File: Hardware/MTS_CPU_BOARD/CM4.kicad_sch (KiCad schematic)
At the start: 1 part

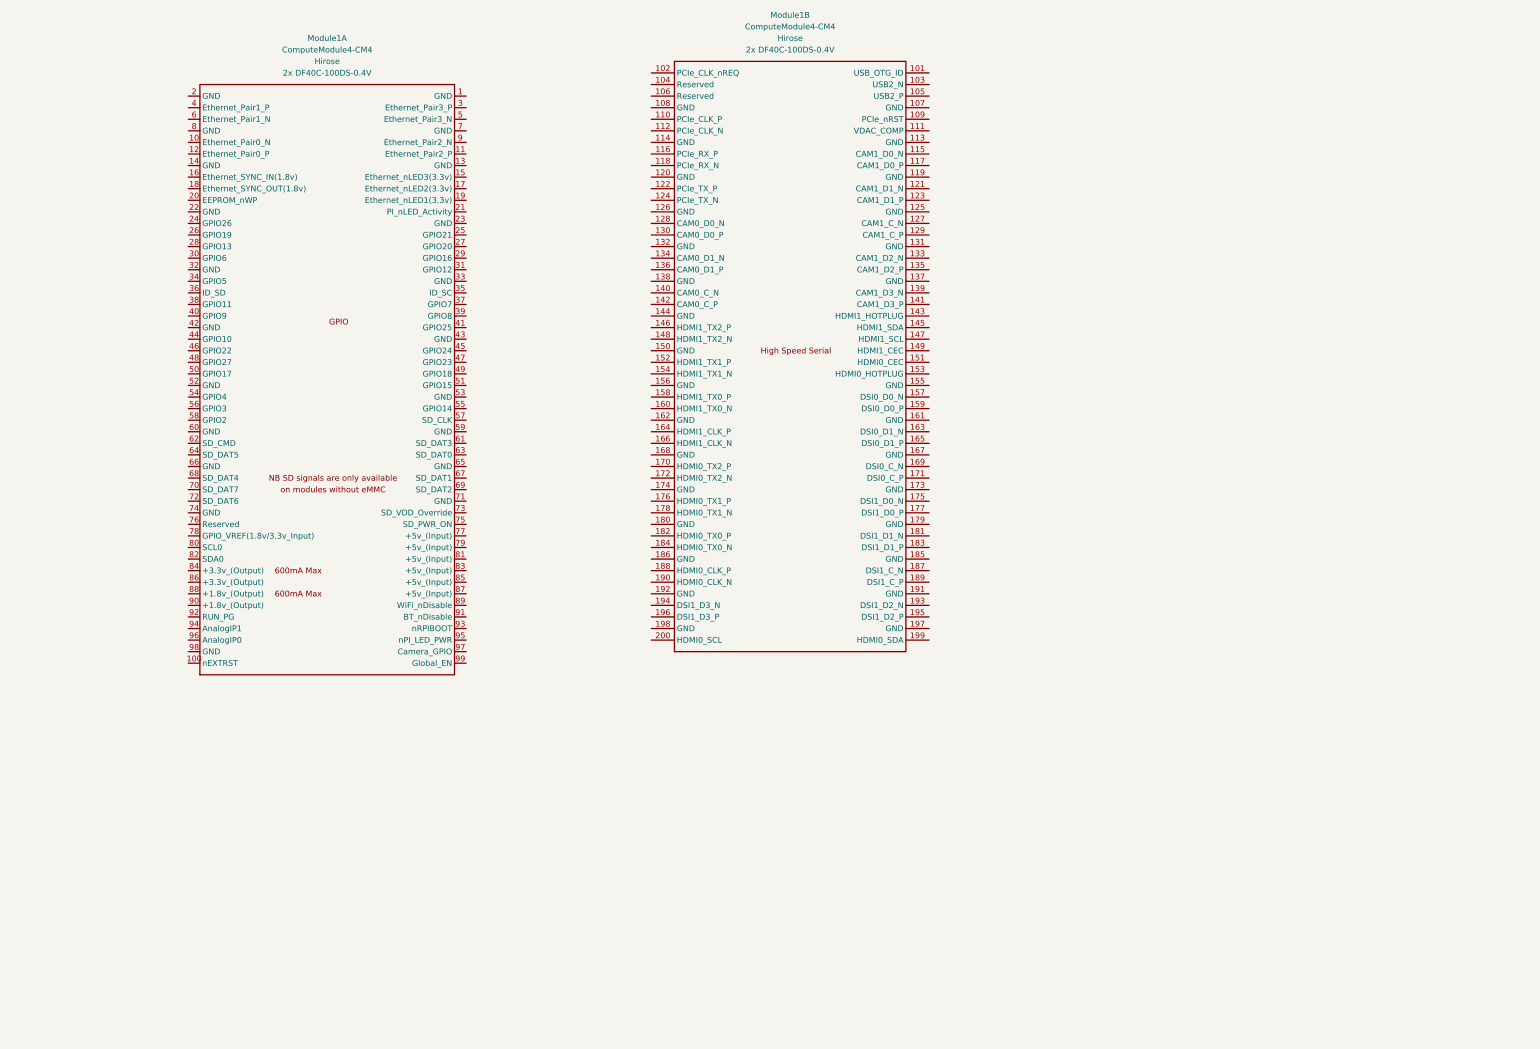
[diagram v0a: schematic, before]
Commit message: Add EtherCAT
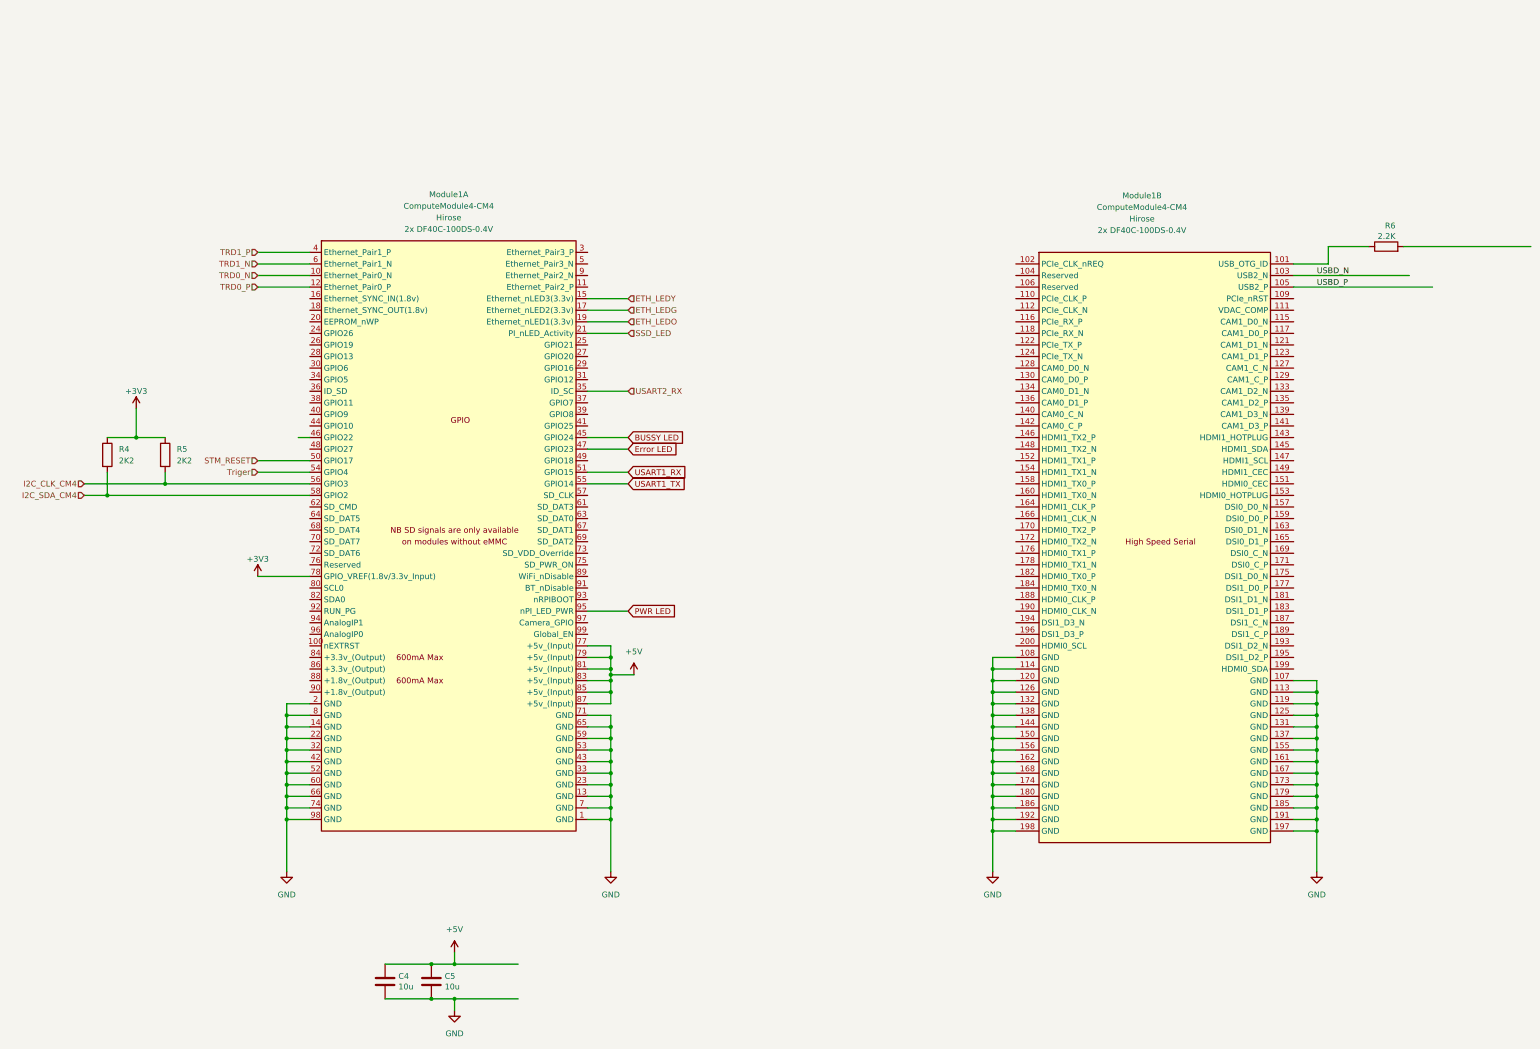
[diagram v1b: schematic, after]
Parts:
- added C4, C5: 10u, Capacitor_SMD:C_0805_2012Metric, symbol Device:C
- added R4, R5: 2K2, Resistor_SMD:R_0603_1608Metric, symbol Device:R
- added R6: 2.2K, Resistor_SMD:R_0603_1608Metric, symbol Device:R
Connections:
- net GND: now reaches Module1.1 (GND)
- net GND: now also Module1.107 (GND), Module1.108 (GND), Module1.113 (GND), Module1.114 (GND), Module1.119 (GND), Module1.120 (GND), Module1.125 (GND), Module1.126 (GND), Module1.13 (GND), Module1.131 (GND), Module1.132 (GND), Module1.137 (GND), Module1.138 (GND), Module1.14 (GND), Module1.144 (GND), Module1.150 (GND), Module1.155 (GND), Module1.156 (GND), Module1.161 (GND), Module1.162 (GND), Module1.167 (GND), Module1.168 (GND), Module1.173 (GND), Module1.174 (GND), Module1.179 (GND), Module1.180 (GND), Module1.185 (GND), Module1.186 (GND), Module1.191 (GND), Module1.192 (GND), Module1.197 (GND), Module1.198 (GND), Module1.2 (GND), Module1.22 (GND), Module1.23 (GND), Module1.32 (GND), Module1.33 (GND), Module1.42 (GND), Module1.43 (GND), Module1.52 (GND), Module1.53 (GND), Module1.59 (GND), Module1.60 (GND), Module1.65 (GND), Module1.66 (GND), Module1.7 (GND), Module1.71 (GND), Module1.74 (GND), Module1.8 (GND), Module1.98 (GND), C4.2, C5.2
- net TRD0_N: now reaches Module1.10 (Ethernet_Pair0_N)
- net TRD0_P: now reaches Module1.12 (Ethernet_Pair0_P)
- net ETH_LEDY: now reaches Module1.15 (Ethernet_nLED3(3.3v))
- net ETH_LEDG: now reaches Module1.17 (Ethernet_nLED2(3.3v))
- net ETH_LEDO: now reaches Module1.19 (Ethernet_nLED1(3.3v))
- net SSD_LED: now reaches Module1.21 (PI_nLED_Activity)
- net USART2_RX: now reaches Module1.35 (ID_SC)
- net TRD1_P: now reaches Module1.4 (Ethernet_Pair1_P)
- net BUSSY LED: now reaches Module1.45 (GPIO24)
- net Error LED: now reaches Module1.47 (GPIO23)
- net STM_RESET: now reaches Module1.50 (GPIO17)
- net USART1_RX: now reaches Module1.51 (GPIO15)
- net Triger: now reaches Module1.54 (GPIO4)
- net USART1_TX: now reaches Module1.55 (GPIO14)
- net I2C_CLK_CM4: now reaches Module1.56 (GPIO3)
- net I2C_CLK_CM4: now also R5.2
- net I2C_SDA_CM4: now reaches Module1.58 (GPIO2)
- net I2C_SDA_CM4: now also R4.2
- net TRD1_N: now reaches Module1.6 (Ethernet_Pair1_N)
- net +5V: now reaches Module1.77 (+5v_(Input))
- net +5V: now also Module1.79 (+5v_(Input)), Module1.81 (+5v_(Input)), Module1.83 (+5v_(Input)), Module1.85 (+5v_(Input)), Module1.87 (+5v_(Input)), C4.1, C5.1
- net +3V3: now reaches Module1.78 (GPIO_VREF(1.8v/3.3v_Input))
- net +3V3: now also R4.1, R5.1
- net PWR LED: now reaches Module1.95 (nPI_LED_PWR)
- net at Module1.101 (USB_OTG_ID): now also R6.1
- net USBD_N: now reaches Module1.103 (USB2_N)
- net USBD_P: now reaches Module1.105 (USB2_P)

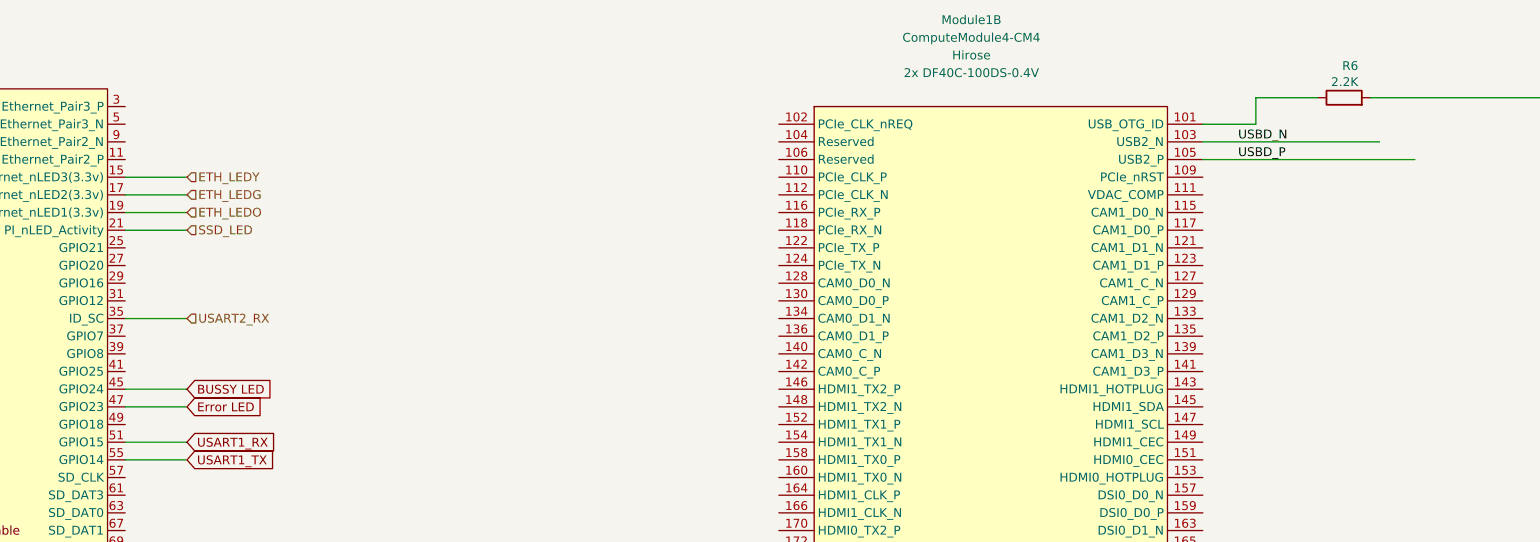
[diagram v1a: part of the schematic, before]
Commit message: Add status Led´s
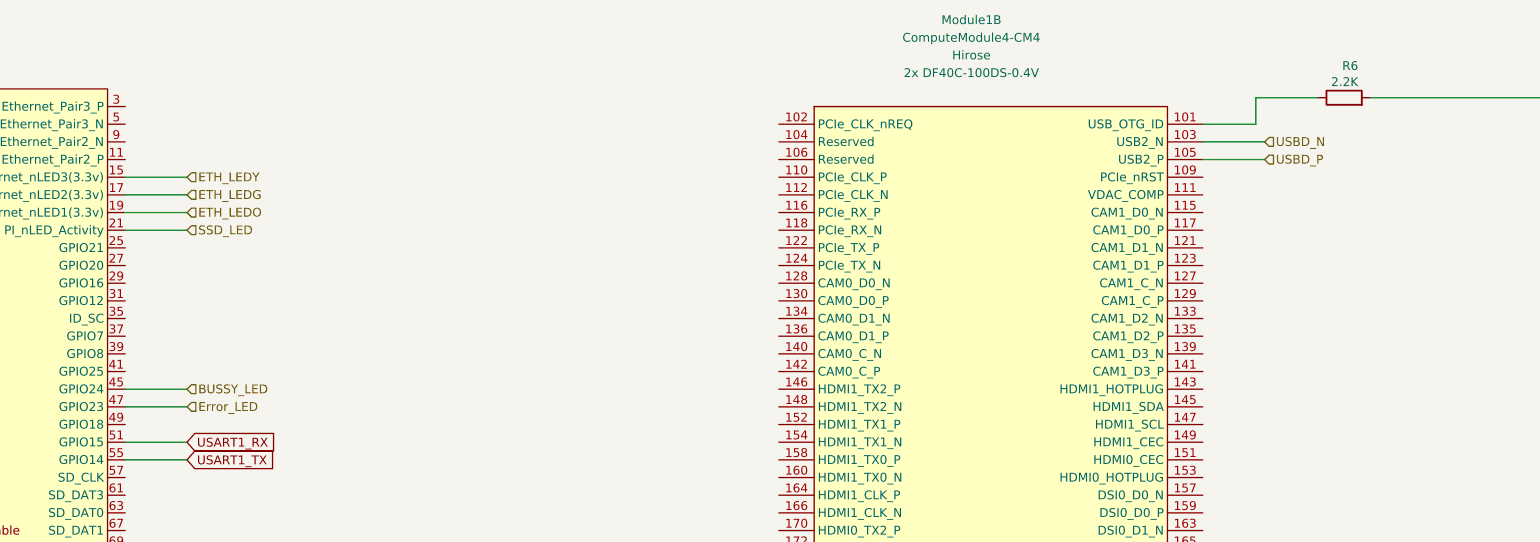
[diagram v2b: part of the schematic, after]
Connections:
- net BUSSY LED renamed BUSSY_LED
- net Error LED renamed Error_LED
- net USART2_RX: no longer names the net of Module1.35 (ID_SC)
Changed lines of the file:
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@@
-	(wire
-		(pts
-			(xy 149.86 96.52) (xy 140.97 96.52)
-		)
-		(stroke
-			(width 0)
-			(type default)
-		)
-	)
 	(wire
 		(pts
@@
 	(wire
 		(pts
-			(xy 295.91 73.66) (xy 326.39 73.66)
+			(xy 295.91 73.66) (xy 304.8 73.66)
 		)
 		(stroke
@@
 	(wire
 		(pts
-			(xy 295.91 71.12) (xy 321.31 71.12)
+			(xy 295.91 71.12) (xy 304.8 71.12)
 		)
 		(stroke
@@
 			(width 0)
 			(type default)
-		)
-	)
-	(label "USBD_P"
-		(at 300.99 73.66 0)
-		(effects
-			(font
-				(size 1.27 1.27)
-			)
-			(justify left bottom)
-		)
-	)
-	(label "USBD_N"
-		(at 300.99 71.12 0)
-		(effects
-			(font
-				(size 1.27 1.27)
-			)
-			(justify left bottom)
-		)
-	)
-	(global_label "BUSSY LED"
-		(shape input)
-		(at 149.86 106.68 0)
-		(fields_autoplaced yes)
-		(effects
-			(font
-				(size 1.27 1.27)
-			)
-			(justify left)
-		)
-		(property "Intersheetrefs" "${INTERSHEET_REFS}"
-			(at 163.4631 106.68 0)
-			(effects
-				(font
-					(size 1.27 1.27)
-				)
-				(justify left)
-				(hide yes)
-			)
 		)
 	)
@@
 		)
 	)
-	(global_label "Error LED"
-		(shape input)
-		(at 149.86 109.22 0)
-		(fields_autoplaced yes)
-		(effects
-			(font
-				(size 1.27 1.27)
-			)
-			(justify left)
-		)
-		(property "Intersheetrefs" "${INTERSHEET_REFS}"
-			(at 162.0116 109.22 0)
-			(effects
-				(font
-					(size 1.27 1.27)
-				)
-				(justify left)
-				(hide yes)
-			)
-		)
-	)
 	(global_label "USART1_TX"
 		(shape input)
@@
 		)
 	)
-	(hierarchical_label "USART2_RX"
+	(hierarchical_label "USBD_P"
 		(shape input)
-		(at 149.86 96.52 0)
+		(at 304.8 73.66 0)
 		(effects
 			(font
@@
 		)
 	)
+	(hierarchical_label "USBD_N"
+		(shape input)
+		(at 304.8 71.12 0)
+		(effects
+			(font
+				(size 1.27 1.27)
+			)
+			(justify left)
+		)
+	)
+	(hierarchical_label "BUSSY_LED"
+		(shape input)
+		(at 149.86 106.68 0)
+		(effects
+			(font
+				(size 1.27 1.27)
+			)
+			(justify left)
+		)
+	)
 	(hierarchical_label "ETH_LEDO"
 		(shape input)
@@
 		)
 	)
+	(hierarchical_label "Error_LED"
+		(shape input)
+		(at 149.86 109.22 0)
+		(effects
+			(font
+				(size 1.27 1.27)
+			)
+			(justify left)
+		)
+	)
